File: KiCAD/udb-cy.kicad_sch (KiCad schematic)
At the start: 15 parts, among them J1 SM04B-SRSS-TB(LF)(SN), J2 USB_C_Receptacle

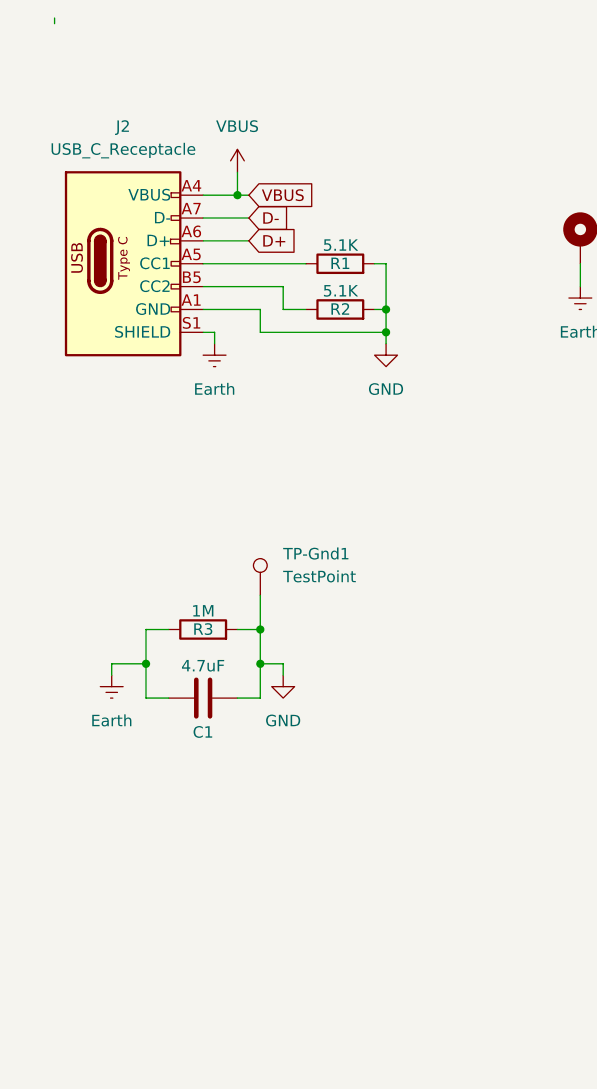
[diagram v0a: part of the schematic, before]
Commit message: Added JST SUR connector option
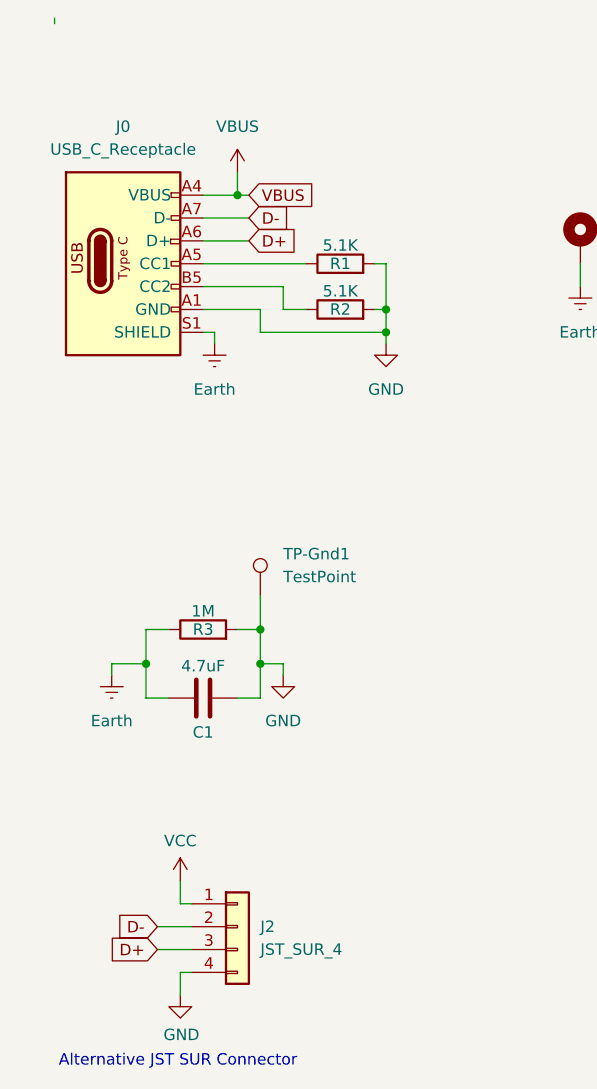
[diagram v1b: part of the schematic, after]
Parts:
- added J2: JST_SUR_4, Connector_JST:JST_SUR_SM04B-SURS-TF_1x04-1MP_P0.80mm_Horizontal, symbol PCM_SparkFun-Connector:Conn_01x04_JST_P1.25mm_Locking_Horizontal_SMD
- renumbered J2 to J0
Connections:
- net D+: now also J2.3 (Pin_3)
- net D-: now also J2.2 (Pin_2)
- net GND: now also J2.4 (Pin_4)
- net VCC: now also J2.1 (Pin_1)
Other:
- note added: "Alternative JST SUR Connector"

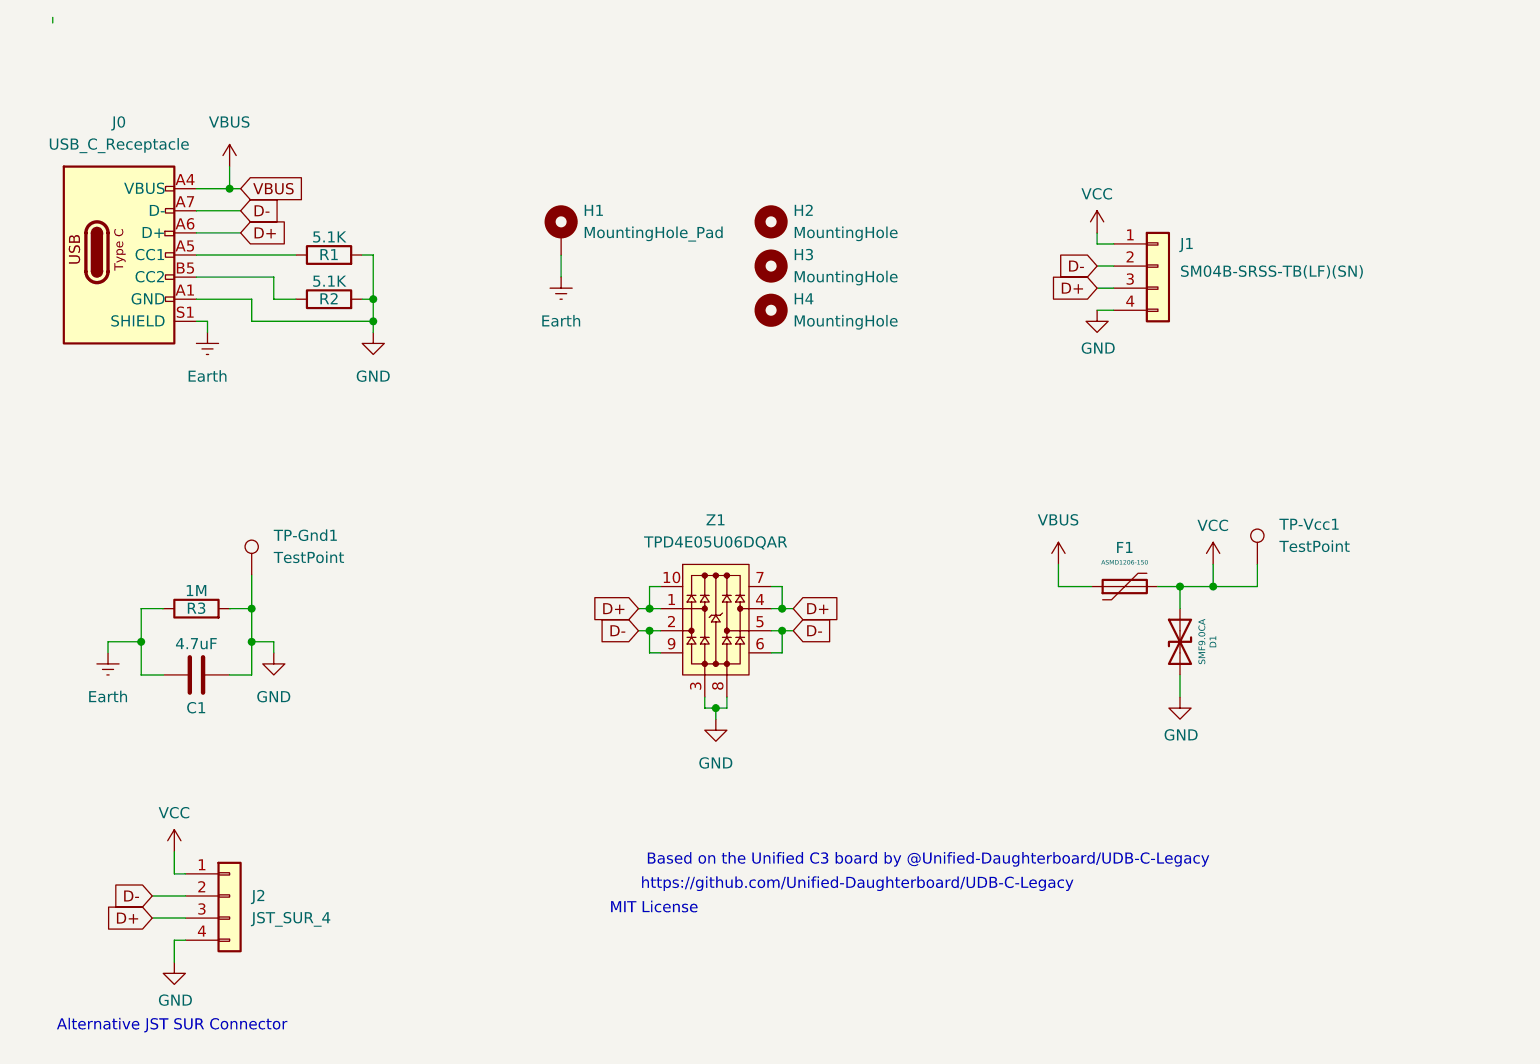
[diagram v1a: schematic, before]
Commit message: Expose all 4 pins on the underside
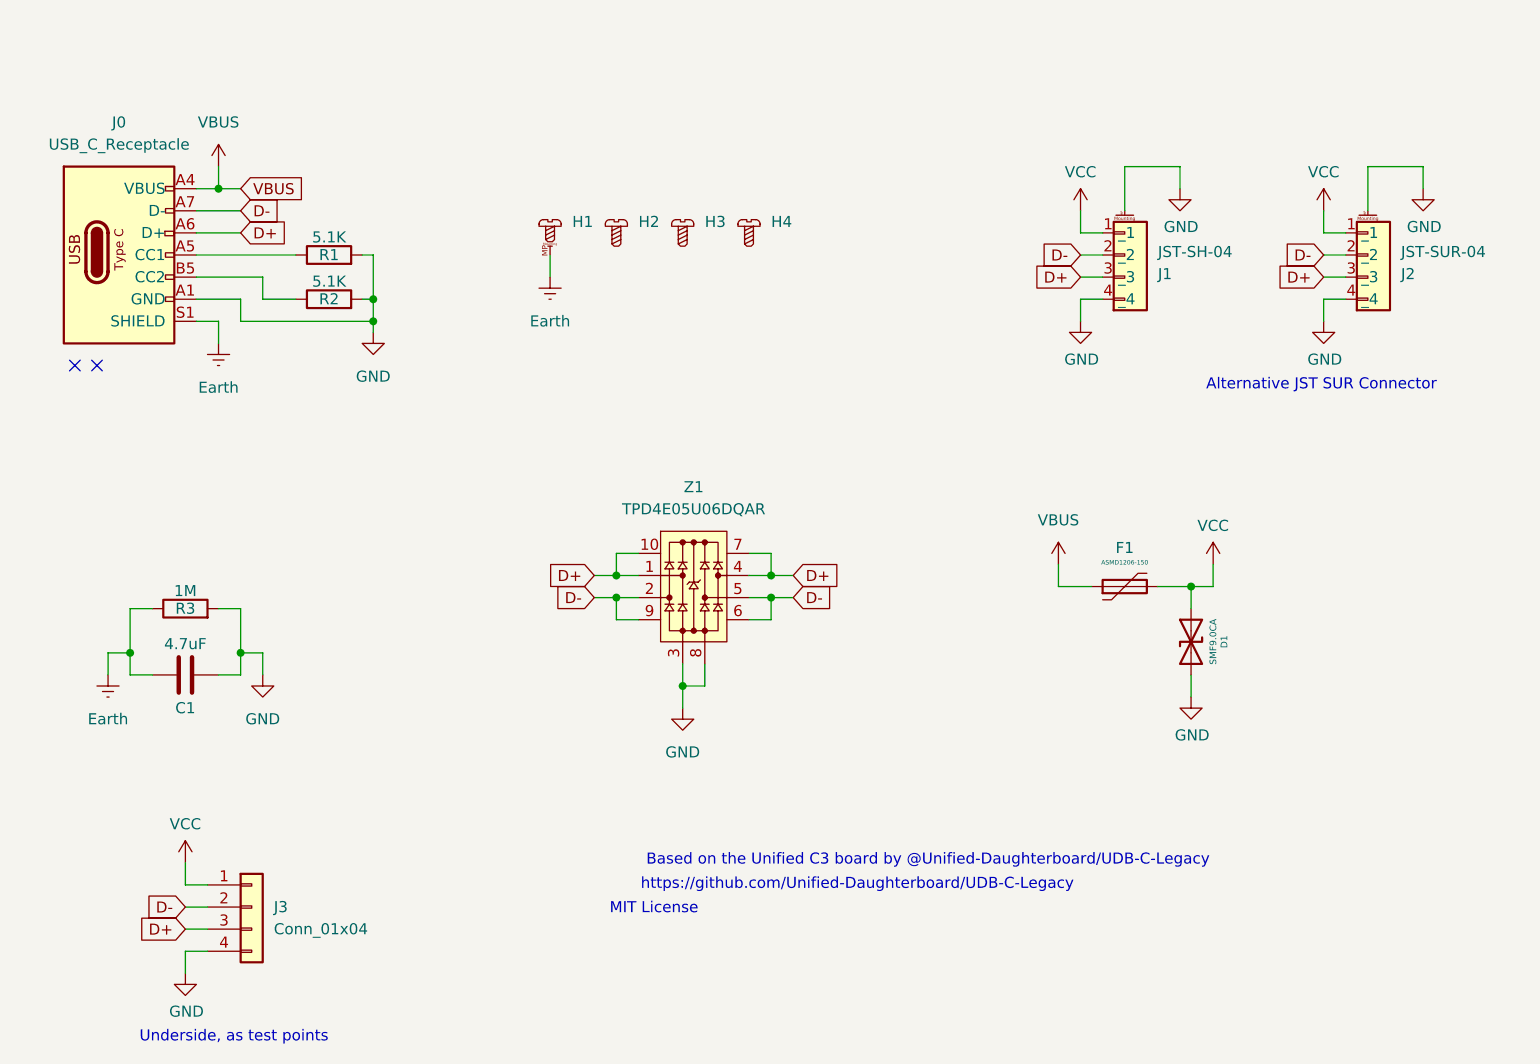
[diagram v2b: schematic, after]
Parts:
- removed H1: MountingHole_Pad, MountingHole:MountingHole_2.2mm_M2_Pad, symbol Mechanical:MountingHole_Pad
- removed H2, H3, H4: MountingHole, MountingHole:MountingHole_2.2mm_M2, symbol Mechanical:MountingHole
- removed J1: SM04B-SRSS-TB(LF)(SN), Connector_JST:JST_SH_SM04B-SRSS-TB_1x04-1MP_P1.00mm_Horizontal, symbol Connector_Generic:Conn_01x04
- removed J2: JST_SUR_4, Connector_JST:JST_SUR_SM04B-SURS-TF_1x04-1MP_P0.80mm_Horizontal, symbol PCM_SparkFun-Connector:Conn_01x04_JST_P1.25mm_Locking_Horizontal_SMD
- removed TP-Gnd1, TP-Vcc1: TestPoint, TestPoint:TestPoint_Pad_1.5x1.5mm, symbol Connector:TestPoint
- added H1: ~, ts-kicad-lib:Mount_M2_Rel, symbol ts-kicad-lib:Mounting_Point
- added H2, H3, H4: ~, ts-kicad-lib:Hole_M2, symbol ts-kicad-lib:Mounting_Hole
- added J1: JST-SH-04, Connector_JST:JST_SH_SM04B-SRSS-TB_1x04-1MP_P1.00mm_Horizontal, symbol ts-kicad-lib:CONN_04
- added J2: JST-SUR-04, Connector_JST:JST_SUR_SM04B-SURS-TF_1x04-1MP_P0.80mm_Horizontal, symbol ts-kicad-lib:CONN_04
- added J3: Conn_01x04, PCM_SparkFun-Connector:1x04_P2.54mm_SolderPads, symbol PCM_SparkFun-Connector:Conn_01x04_P2.54mm
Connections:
- net D+: now also J1.3 (_3), J2.3 (_3), J3.3 (Pin_3)
- net D-: now also J1.2 (_2), J2.2 (_2), J3.2 (Pin_2)
- net Earth: now also H1.MP
- net GND: now also J1.4 (_4), J1.MP, J2.4 (_4), J2.MP, J3.4 (Pin_4)
- net VCC: now also J1.1 (_1), J2.1 (_1), J3.1 (Pin_1)
- no-connect marks 0 -> 2
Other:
- note added: "Underside, as test points"
- moved on the sheet: C1, D1, R3, Z1

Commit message: update-2025-11-20
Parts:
- J1: symbol ts-kicad-lib:CONN_04 -> ts-keyboard-lib:CONN_UDB
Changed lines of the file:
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@@
+	)
+	(junction
+		(at 144.78 48.26)
+		(diameter 0)
+		(color 0 0 0 0)
 	)
 	(junction
@@
 	(wire
 		(pts
-			(xy 147.32 45.72) (xy 147.32 43.18)
+			(xy 144.78 49.53) (xy 144.78 48.26)
 		)
 		(stroke
@@
 	(wire
 		(pts
-			(xy 152.4 27.94) (xy 152.4 33.02)
-		)
-		(stroke
-			(width 0)
-			(type default)
-		)
-	)
-	(wire
-		(pts
 			(xy 38.1 78.74) (xy 38.1 83.82)
 		)
@@
 	(wire
 		(pts
+			(xy 144.78 48.26) (xy 142.24 48.26)
+		)
+		(stroke
+			(width 0)
+			(type default)
+		)
+	)
+	(wire
+		(pts
 			(xy 144.78 76.2) (xy 148.59 76.2)
 		)
@@
 	(wire
 		(pts
-			(xy 147.32 40.64) (xy 149.86 40.64)
-		)
-		(stroke
-			(width 0)
-			(type default)
-		)
-	)
-	(wire
-		(pts
 			(xy 156.21 76.2) (xy 160.02 76.2)
 		)
@@
 	(wire
 		(pts
+			(xy 147.32 45.72) (xy 147.32 48.26)
+		)
+		(stroke
+			(width 0)
+			(type default)
+		)
+	)
+	(wire
+		(pts
 			(xy 45.72 43.18) (xy 50.8 43.18)
 		)
@@
 	(wire
 		(pts
+			(xy 142.24 43.18) (xy 144.78 43.18)
+		)
+		(stroke
+			(width 0)
+			(type default)
+		)
+	)
+	(wire
+		(pts
 			(xy 180.34 27.94) (xy 180.34 33.02)
 		)
@@
 	(wire
 		(pts
+			(xy 144.78 48.26) (xy 147.32 48.26)
+		)
+		(stroke
+			(width 0)
+			(type default)
+		)
+	)
+	(wire
+		(pts
 			(xy 66.04 45.72) (xy 50.8 45.72)
 		)
@@
 	(wire
 		(pts
-			(xy 158.75 27.94) (xy 152.4 27.94)
-		)
-		(stroke
-			(width 0)
-			(type default)
-		)
-	)
-	(wire
-		(pts
-			(xy 147.32 33.02) (xy 147.32 35.56)
+			(xy 142.24 33.02) (xy 142.24 35.56)
 		)
 		(stroke
@@
 	(wire
 		(pts
+			(xy 142.24 38.1) (xy 144.78 38.1)
+		)
+		(stroke
+			(width 0)
+			(type default)
+		)
+	)
+	(wire
+		(pts
 			(xy 48.26 86.36) (xy 50.8 86.36)
 		)
@@
 	(wire
 		(pts
+			(xy 142.24 48.26) (xy 142.24 43.18)
+		)
+		(stroke
+			(width 0)
+			(type default)
+		)
+	)
+	(wire
+		(pts
 			(xy 109.22 80.01) (xy 111.76 80.01)
 		)
@@
 	(wire
 		(pts
-			(xy 158.75 30.48) (xy 158.75 27.94)
-		)
-		(stroke
-			(width 0)
-			(type default)
-		)
-	)
-	(wire
-		(pts
-			(xy 147.32 35.56) (xy 149.86 35.56)
-		)
-		(stroke
-			(width 0)
-			(type default)
-		)
-	)
-	(wire
-		(pts
 			(xy 48.26 30.48) (xy 50.8 30.48)
 		)
@@
 	(wire
 		(pts
+			(xy 142.24 35.56) (xy 144.78 35.56)
+		)
+		(stroke
+			(width 0)
+			(type default)
+		)
+	)
+	(wire
+		(pts
 			(xy 40.64 78.74) (xy 38.1 78.74)
 		)
@@
 	(wire
 		(pts
-			(xy 147.32 43.18) (xy 149.86 43.18)
-		)
-		(stroke
-			(width 0)
-			(type default)
-		)
-	)
-	(wire
-		(pts
-			(xy 149.86 38.1) (xy 147.32 38.1)
+			(xy 142.24 40.64) (xy 144.78 40.64)
 		)
 		(stroke
@@
 	(global_label "D+"
 		(shape input)
-		(at 147.32 40.64 180)
+		(at 142.24 40.64 180)
 		(effects
 			(font
@@
 		)
 		(property "Intersheetrefs" "${INTERSHEET_REFS}"
-			(at 147.32 40.64 0)
+			(at 142.24 40.64 0)
 			(effects
 				(font
@@
 	(global_label "D-"
 		(shape input)
-		(at 147.32 38.1 180)
+		(at 142.24 38.1 180)
 		(effects
 			(font
@@
 		)
 		(property "Intersheetrefs" "${INTERSHEET_REFS}"
-			(at 147.32 38.1 0)
+			(at 142.24 38.1 0)
 			(effects
 				(font
@@
 	(symbol
 		(lib_id "power:GND")
-		(at 147.32 45.72 0)
+		(at 144.78 49.53 0)
 		(unit 1)
 		(exclude_from_sim no)
@@
 		(dnp no)
 		(property "Reference" "#PWR0104"
-			(at 147.32 52.07 0)
+			(at 144.78 55.88 0)
 			(effects
 				(font
@@
 		)
 		(property "Value" "GND"
-			(at 147.447 50.1142 0)
+			(at 144.907 53.9242 0)
 			(effects
 				(font
@@
 		)
 		(property "Footprint" ""
-			(at 147.32 45.72 0)
+			(at 144.78 49.53 0)
 			(effects
 				(font
@@
 		)
 		(property "Datasheet" ""
-			(at 147.32 45.72 0)
+			(at 144.78 49.53 0)
 			(effects
 				(font
@@
 		)
 		(property "Description" ""
-			(at 147.32 45.72 0)
+			(at 144.78 49.53 0)
 			(effects
 				(font
@@
 	(symbol
 		(lib_id "power:VCC")
-		(at 147.32 33.02 0)
+		(at 142.24 33.02 0)
 		(unit 1)
 		(exclude_from_sim no)
@@
 		(dnp no)
 		(property "Reference" "#PWR0103"
-			(at 147.32 36.83 0)
+			(at 142.24 36.83 0)
 			(effects
 				(font
@@
 		)
 		(property "Value" "VCC"
-			(at 147.32 28.575 0)
+			(at 142.24 28.575 0)
 			(effects
 				(font
@@
 		)
 		(property "Footprint" ""
-			(at 147.32 33.02 0)
+			(at 142.24 33.02 0)
 			(effects
 				(font
@@
 		)
 		(property "Datasheet" ""
-			(at 147.32 33.02 0)
+			(at 142.24 33.02 0)
 			(effects
 				(font
@@
 		)
 		(property "Description" ""
-			(at 147.32 33.02 0)
+			(at 142.24 33.02 0)
 			(effects
 				(font
@@
 	)
 	(symbol
-		(lib_id "ts-kicad-lib:CONN_04")
-		(at 152.4 38.1 0)
-		(mirror x)
+		(lib_id "ts-keyboard-lib:CONN_UDB")
+		(at 147.32 40.64 0)
 		(unit 1)
 		(exclude_from_sim no)
@@
 		(dnp no)
 		(property "Reference" "J1"
-			(at 156.21 40.2845 0)
+			(at 152.4 38.1 0)
 			(effects
 				(font
@@
 		)
 		(property "Value" "JST-SH-04"
-			(at 156.21 37.7445 0)
+			(at 152.4 40.64 0)
 			(effects
 				(font
@@
 		)
 		(property "Footprint" "Connector_JST:JST_SH_SM04B-SRSS-TB_1x04-1MP_P1.00mm_Horizontal"
-			(at 152.4 38.1 0)
-			(effects
-				(font
-					(size 1.27 1.27)
-				)
-				(hide yes)
-			)
-		)
-		(property "Datasheet" ""
-			(at 152.4 38.1 0)
-			(effects
-				(font
-					(size 1.27 1.27)
-				)
-				(hide yes)
-			)
-		)
-		(property "Description" ""
-			(at 152.4 38.1 0)
+			(at 147.32 27.94 0)
+			(effects
+				(font
+					(size 1.27 1.27)
+				)
+				(hide yes)
+			)
+		)
+		(property "Datasheet" "https://unified-daughterboard.github.io"
+			(at 147.32 30.48 0)
+			(effects
+				(font
+					(size 1.27 1.27)
+				)
+				(hide yes)
+			)
+		)
+		(property "Description" "Unified Daughterboard C Series"
+			(at 147.32 25.4 0)
 			(effects
 				(font
@@
 					(unit 1)
 				)
-			)
-		)
-	)
-	(symbol
-		(lib_id "power:GND")
-		(at 158.75 30.48 0)
-		(unit 1)
-		(exclude_from_sim no)
-		(in_bom yes)
-		(on_board yes)
-		(dnp no)
-		(property "Reference" "#PWR013"
-			(at 158.75 36.83 0)
-			(effects
-				(font
-					(size 1.27 1.27)
-				)
-				(hide yes)
-			)
-		)
-		(property "Value" "GND"
-			(at 158.877 34.8742 0)
-			(effects
-				(font
-					(size 1.27 1.27)
-				)
-			)
-		)
-		(property "Footprint" ""
-			(at 158.75 30.48 0)
-			(effects
-				(font
-					(size 1.27 1.27)
-				)
-				(hide yes)
-			)
-		)
-		(property "Datasheet" ""
-			(at 158.75 30.48 0)
-			(effects
-				(font
-					(size 1.27 1.27)
-				)
-				(hide yes)
-			)
-		)
-		(property "Description" ""
-			(at 158.75 30.48 0)
-			(effects
-				(font
-					(size 1.27 1.27)
-				)
-			)
-		)
-		(pin "1"
-		)
-		(instances
-			(project "udb-cy"
-				(path "/45b81b3f-a376-44a8-a955-c3164d7947b8"
-					(reference "#PWR013")
-					(unit 1)
-				)

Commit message: .
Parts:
- added C2: 1nF, Capacitor_SMD:C_0603_1608Metric, symbol Device:C
- added FB1: 600Ω @ 100MHz, Inductor_SMD:L_0603_1608Metric, symbol ts-kicad-lib:Ferrite_Bead
- C1: value 4.7uF -> 0.1µF
- H1, H2, H3, H4: value ~ -> (none)
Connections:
- net Earth: now also C2.1, FB1.1
- net GND: now also C2.2, FB1.2
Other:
- moved on the sheet: R3

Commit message: updated
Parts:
- J1: footprint Connector_JST:JST_SH_SM04B-SRSS-TB_1x04-1MP_P1.00mm_Horizontal -> ts-keyboard-lib:JST_SH_SM04B-SRSS-TB_1x04-1MP_P1.00mm_Horizontal
- R1, R2, R3: footprint Resistors_SMD:R_0603 -> Resistor_SMD:R_0603_1608Metric_Pad0.98x0.95mm_HandSolder
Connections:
- net Earth: now also J0.SH (SHIELD); no longer J0.S1 (SHIELD)
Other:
- moved on the sheet: D1, F1, H1, H2, H4, J3, Z1
